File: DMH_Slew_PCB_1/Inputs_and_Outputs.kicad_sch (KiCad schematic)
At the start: 21 parts, among them J1 TS_Jack_6.35mm_Sw, J10 TS_Jack_6.35mm_Sw, J11 TS_Jack_6.35mm_Sw, J12 TS_Jack_6.35mm_Sw, J2 TS_Jack_6.35mm_Sw, J200 IDC_02x05, J3 TS_Jack_6.35mm_Sw, J5 TS_Jack_6.35mm_Sw, J6 TS_Jack_6.35mm_Sw, J7 TS_Jack_6.35mm_Sw, J8 TS_Jack_6.35mm_Sw, J9 TS_Jack_6.35mm_Sw, U1 TL074, U2 TL074

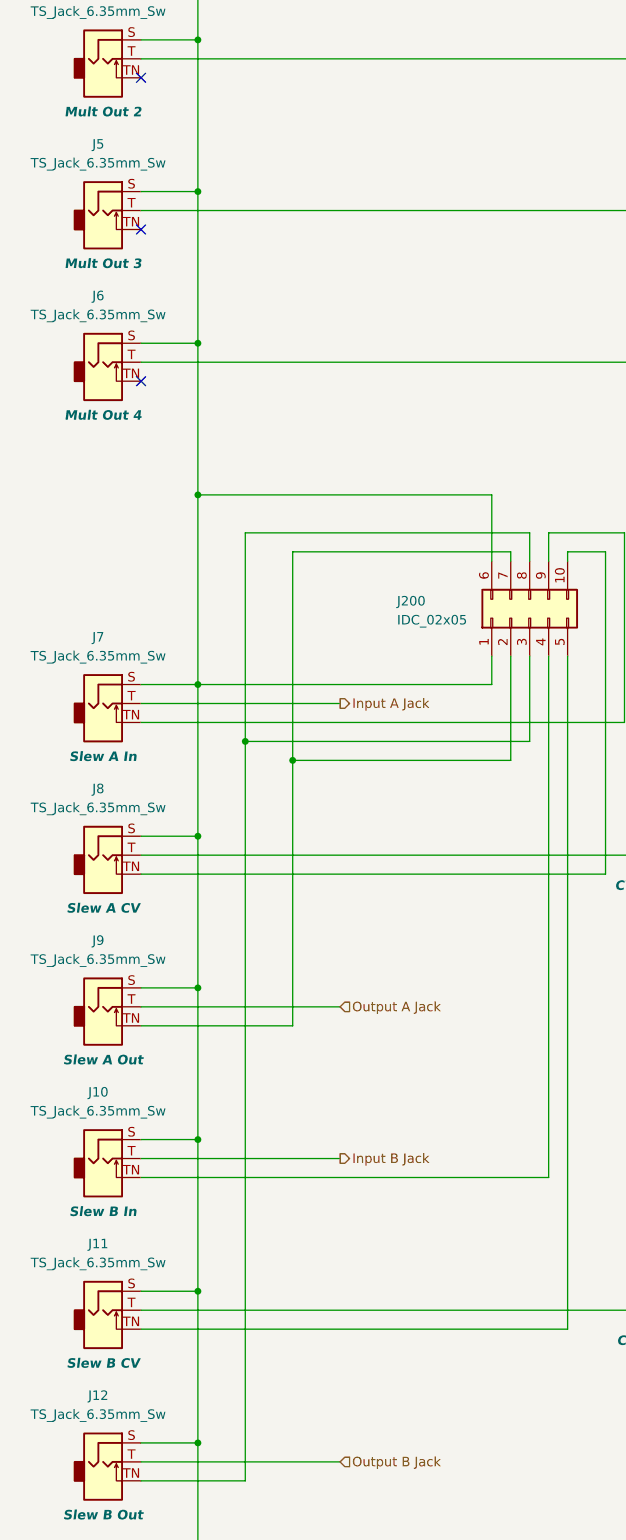
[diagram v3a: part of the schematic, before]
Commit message: Update Inputs_and_Outputs.kicad_sch
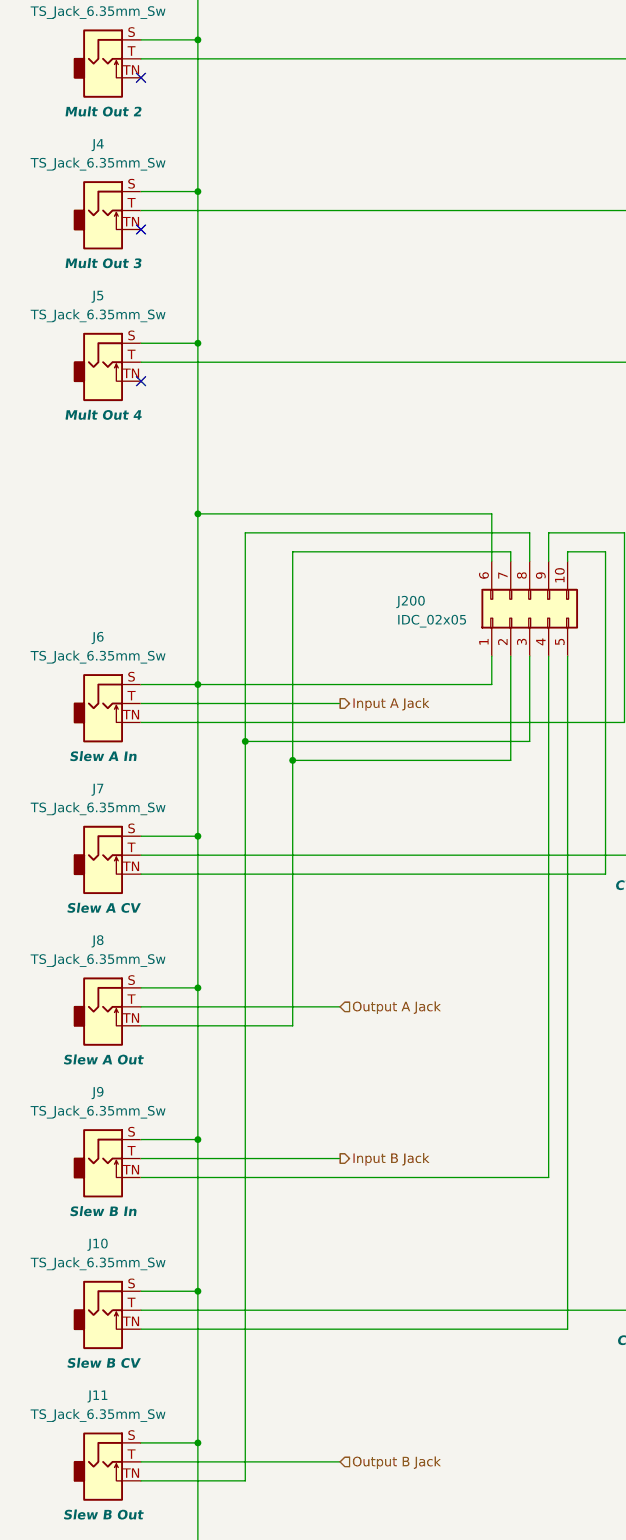
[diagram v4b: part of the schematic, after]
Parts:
- renumbered J11 to J10, J12 to J11, J5 to J4, J6 to J5, J7 to J6, J8 to J7, J9 to J8, J10 to J9
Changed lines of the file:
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@@
 	)
 	(junction
-		(at 38.1 124.46)
-		(diameter 0)
-		(color 0 0 0 0)
-	)
-	(junction
 		(at 114.3 76.2)
 		(diameter 0)
@@
 	)
 	(junction
+		(at 38.1 127)
+		(diameter 0)
+		(color 0 0 0 0)
+	)
+	(junction
 		(at 121.92 233.68)
 		(diameter 0)
@@
 	(wire
 		(pts
-			(xy 77.47 124.46) (xy 38.1 124.46)
+			(xy 77.47 127) (xy 38.1 127)
 		)
 		(stroke
@@
 	(wire
 		(pts
-			(xy 77.47 133.35) (xy 77.47 124.46)
+			(xy 77.47 133.35) (xy 77.47 127)
 		)
 		(stroke
@@
 	(wire
 		(pts
+			(xy 38.1 104.14) (xy 38.1 127)
+		)
+		(stroke
+			(width 0)
+			(type default)
+		)
+	)
+	(wire
+		(pts
 			(xy 114.3 35.56) (xy 114.3 25.4)
 		)
@@
 	(wire
 		(pts
-			(xy 38.1 149.86) (xy 38.1 124.46)
+			(xy 38.1 149.86) (xy 38.1 127)
 		)
 		(stroke
@@
 	(wire
 		(pts
-			(xy 38.1 104.14) (xy 38.1 124.46)
-		)
-		(stroke
-			(width 0)
-			(type default)
-		)
-	)
-	(wire
-		(pts
 			(xy 38.1 210.82) (xy 38.1 190.5)
 		)
@@
 		(on_board yes)
 		(dnp no)
-		(property "Reference" "J11"
+		(property "Reference" "J10"
 			(at 24.765 224.79 0)
 			(effects
@@
 			(project "DMH_Slew_PCB_1"
 				(path "/58f4306d-5387-4983-bb08-41a2313fd315/ce3fef8b-9f1d-4178-b50b-4a046c030679"
-					(reference "J11")
+					(reference "J10")
 					(unit 1)
 				)
@@
 		(on_board yes)
 		(dnp no)
-		(property "Reference" "J12"
+		(property "Reference" "J11"
 			(at 24.765 245.11 0)
 			(effects
@@
 			(project "DMH_Slew_PCB_1"
 				(path "/58f4306d-5387-4983-bb08-41a2313fd315/ce3fef8b-9f1d-4178-b50b-4a046c030679"
-					(reference "J12")
+					(reference "J11")
 					(unit 1)
 				)
@@
 		(on_board yes)
 		(dnp no)
-		(property "Reference" "J8"
+		(property "Reference" "J7"
 			(at 24.765 163.83 0)
 			(effects
@@
 			(project "DMH_Slew_PCB_1"
 				(path "/58f4306d-5387-4983-bb08-41a2313fd315/ce3fef8b-9f1d-4178-b50b-4a046c030679"
-					(reference "J8")
+					(reference "J7")
 					(unit 1)
 				)
@@
 		(on_board yes)
 		(dnp no)
-		(property "Reference" "J5"
+		(property "Reference" "J4"
 			(at 24.765 77.47 0)
 			(effects
@@
 			(project "DMH_Slew_PCB_1"
 				(path "/58f4306d-5387-4983-bb08-41a2313fd315/ce3fef8b-9f1d-4178-b50b-4a046c030679"
-					(reference "J5")
+					(reference "J4")
 					(unit 1)
 				)
@@
 		(on_board yes)
 		(dnp no)
-		(property "Reference" "J7"
+		(property "Reference" "J6"
 			(at 24.765 143.51 0)
 			(effects
@@
 			(project "DMH_Slew_PCB_1"
 				(path "/58f4306d-5387-4983-bb08-41a2313fd315/ce3fef8b-9f1d-4178-b50b-4a046c030679"
-					(reference "J7")
+					(reference "J6")
 					(unit 1)
 				)
@@
 		(on_board yes)
 		(dnp no)
-		(property "Reference" "J6"
+		(property "Reference" "J5"
 			(at 24.765 97.79 0)
 			(effects
@@
 			(project "DMH_Slew_PCB_1"
 				(path "/58f4306d-5387-4983-bb08-41a2313fd315/ce3fef8b-9f1d-4178-b50b-4a046c030679"
-					(reference "J6")
+					(reference "J5")
 					(unit 1)
 				)
@@
 		(on_board yes)
 		(dnp no)
-		(property "Reference" "J9"
+		(property "Reference" "J8"
 			(at 24.765 184.15 0)
 			(effects
@@
 			(project "DMH_Slew_PCB_1"
 				(path "/58f4306d-5387-4983-bb08-41a2313fd315/ce3fef8b-9f1d-4178-b50b-4a046c030679"
-					(reference "J9")
+					(reference "J8")
 					(unit 1)
 				)
@@
 		(on_board yes)
 		(dnp no)
-		(property "Reference" "J10"
+		(property "Reference" "J9"
 			(at 24.765 204.47 0)
 			(effects
@@
 			(project "DMH_Slew_PCB_1"
 				(path "/58f4306d-5387-4983-bb08-41a2313fd315/ce3fef8b-9f1d-4178-b50b-4a046c030679"
-					(reference "J10")
+					(reference "J9")
 					(unit 1)
 				)

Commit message: Core circuit design in progress
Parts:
- removed U2: TL074, Package_DIP:DIP-14_W7.62mm_Socket, symbol Amplifier_Operational:TL074
- added U2: TL072, Package_DIP:DIP-8_W7.62mm_Socket, symbol Amplifier_Operational:TL072
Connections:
- net CV A: now also U2.1
- net CV B: now also U2.7
- net at RV4.2: now also U2.5 (+)
- net at R4.2, RV3.1: now also U2.6 (-)
- net at R3.2, RV1.1: now also U2.2 (-)
- net at RV2.2: now also U2.3 (+)

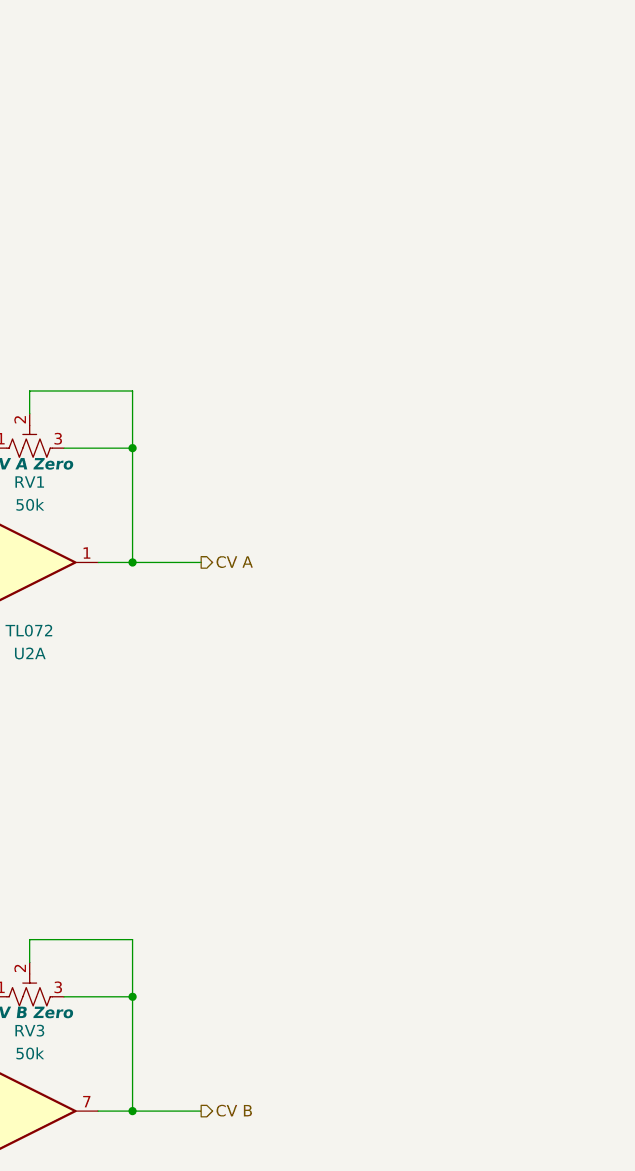
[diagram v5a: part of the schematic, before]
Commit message: Update Inputs_and_Outputs.kicad_sch
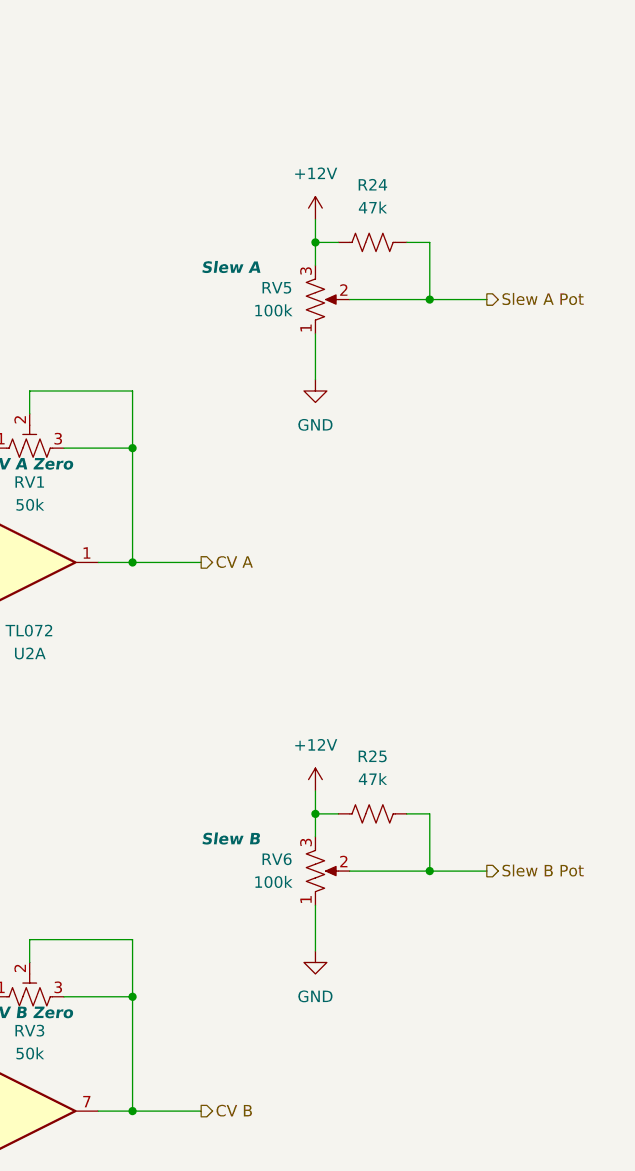
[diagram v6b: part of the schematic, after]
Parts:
- added R24, R25: 47k, Resistor_THT:R_Axial_DIN0207_L6.3mm_D2.5mm_P7.62mm_Horizontal, symbol Device:R_US
- added RV5, RV6: 100k, SynthStuff:Potentiometer_TT_P110KH1, symbol Device:R_Potentiometer_US
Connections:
- net GND: now also RV5.1, RV6.1
- new net +12V: R24.1, R25.1, RV5.3, RV6.3
- new net Slew A Pot: R24.2, RV5.2
- new net Slew B Pot: R25.2, RV6.2

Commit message: Schematic design in progress
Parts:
- removed RV5, RV6: 100k, SynthStuff:Potentiometer_TT_P110KH1, symbol Device:R_Potentiometer_US
- added R26, R27: 47k, Resistor_THT:R_Axial_DIN0207_L6.3mm_D2.5mm_P7.62mm_Horizontal, symbol Device:R_US
- added R48: 100k, Resistor_THT:R_Axial_DIN0207_L6.3mm_D2.5mm_P7.62mm_Horizontal, symbol Device:R_US
- added RV5, RV6: R_Potentiometer_Dual, Potentiometer_THT:Potentiometer_Alpha_RD902F-40-00D_Dual_Vertical, symbol Device:R_Potentiometer_Dual
- added SW3: SW_SPDT, symbol Switch:SW_SPDT
- added U5, U6: CD4053B, Package_DIP:DIP-16_W7.62mm_Socket, symbol Analog_Switch:CD4053B
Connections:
- net +12V: now also R26.1, R27.1, RV5.3, RV5.6, RV6.3, RV6.6
- net GND: now also RV5.1, RV5.4, RV6.1, RV6.4, SW3.1 (A), U5.6 (INH), U5.8 (VSS), U5.9 (S3), U6.6 (INH), U6.8 (VSS), U6.9 (S3)
- net CV A renamed A Rise CV
- net A Rise CV: now also U6.1 (B1), U6.12 (A0)
- net CV B renamed B Fall CV
- net B Fall CV: now also U6.13 (A1), U6.2 (B0)
- net Slew A Pot renamed Slew A Pot G2
- net Slew A Pot G2: now also RV5.5, U5.1 (B1), U5.12 (A0)
- net Slew B Pot renamed A Rise Pot
- net A Rise Pot: now also RV5.2
- new net: R48.1, SW3.2 (B), U5.10 (S2), U5.11 (S1), U6.10 (S2), U6.11 (S1)
- new net +10V: R48.2, U5.16 (VDD), U6.16 (VDD)
- new net -10V: U5.7 (VEE), U6.7 (VEE)
- new net A Fall CV: U6.14 (A)
- new net A Fall Pot: U5.14 (A)
- new net B Fall Pot: R27.2, RV6.2
- new net B Rise CV: U6.15 (B)
- new net B Rise Pot: U5.15 (B)
- new net Slew B Pot G2: R26.2, RV6.5, U5.13 (A1), U5.2 (B0)
- no-connect marks 4 -> 11
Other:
- moved on the sheet: J200, R1, R24, R3, R4, RV1, RV2, RV3, RV4, U1A, U1B, U1C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

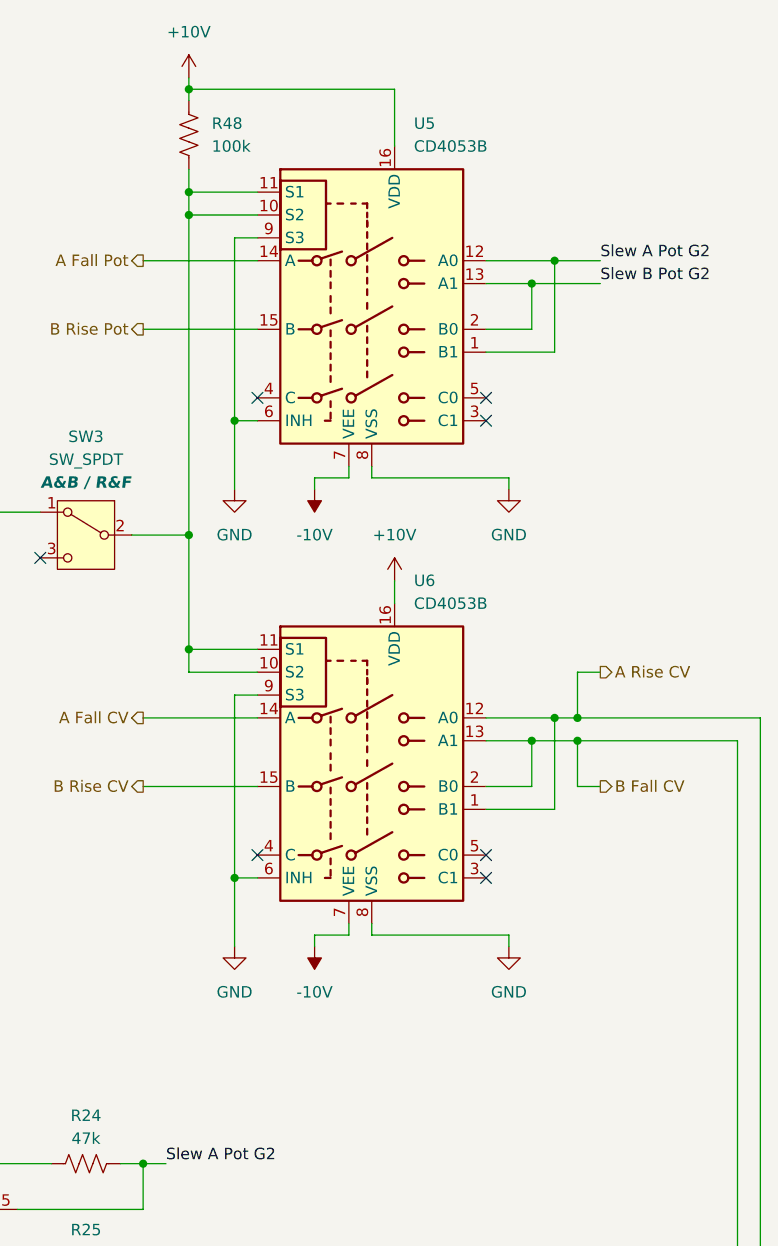
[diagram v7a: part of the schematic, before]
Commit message: Finished power distribution
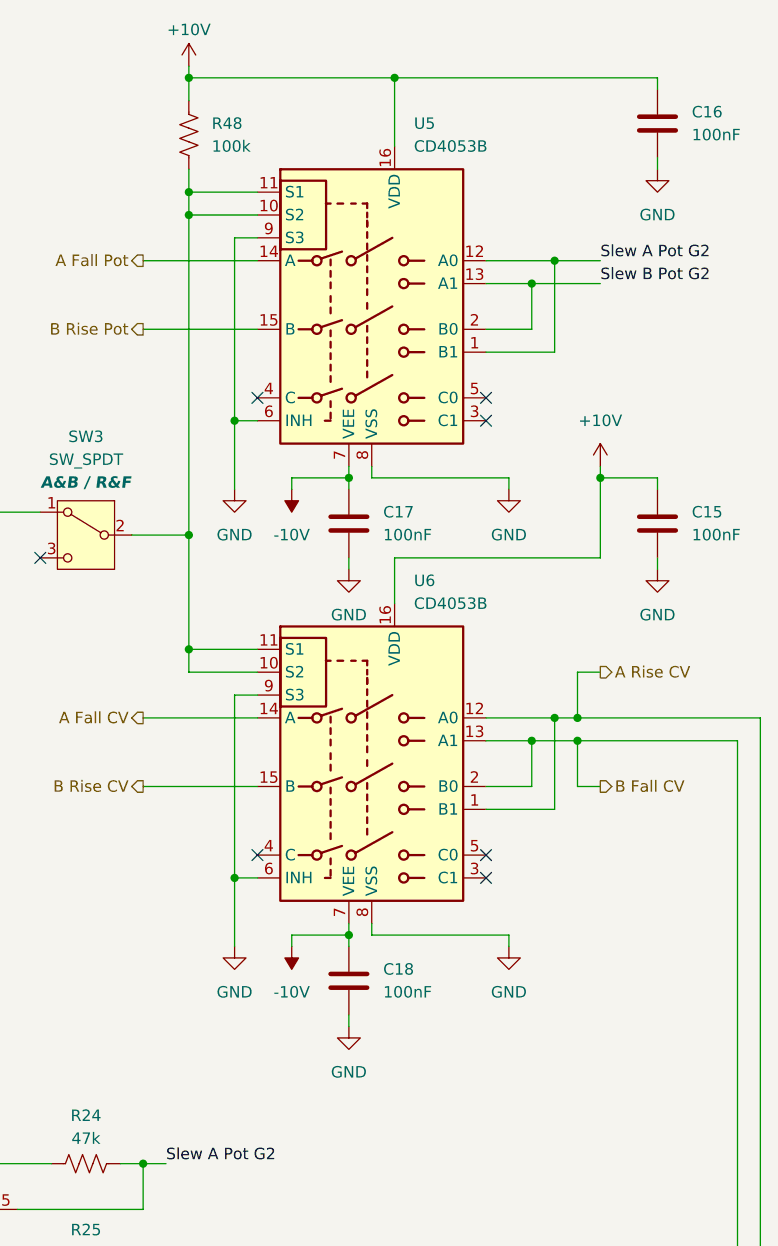
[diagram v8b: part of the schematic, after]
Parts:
- added C15, C16, C17, C18: 100nF, Capacitor_THT:C_Disc_D4.3mm_W1.9mm_P5.00mm, symbol Device:C
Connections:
- net +10V: now also C15.1, C16.1
- net -10V: now also C17.1, C18.1
- net GND: now also C15.2, C16.2, C17.2, C18.2
